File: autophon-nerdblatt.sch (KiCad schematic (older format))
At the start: 2 parts

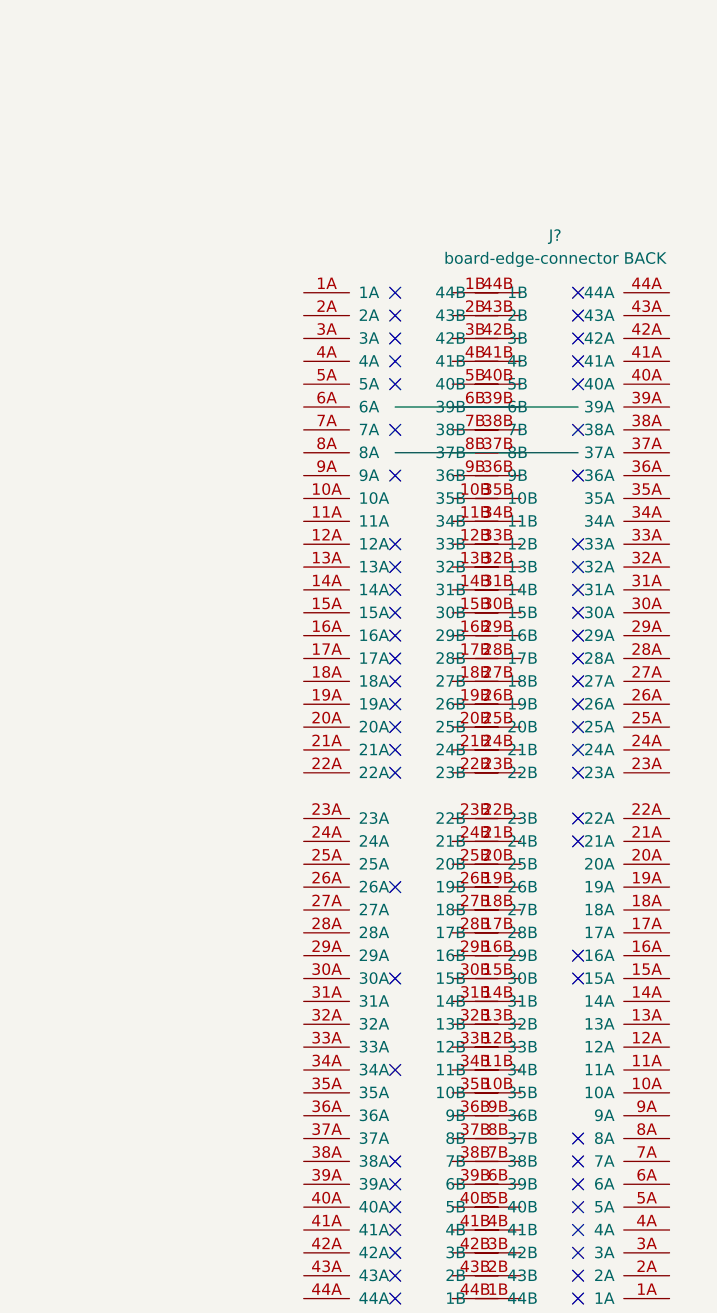
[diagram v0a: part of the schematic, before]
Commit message: measured pinout, added lables accordingly
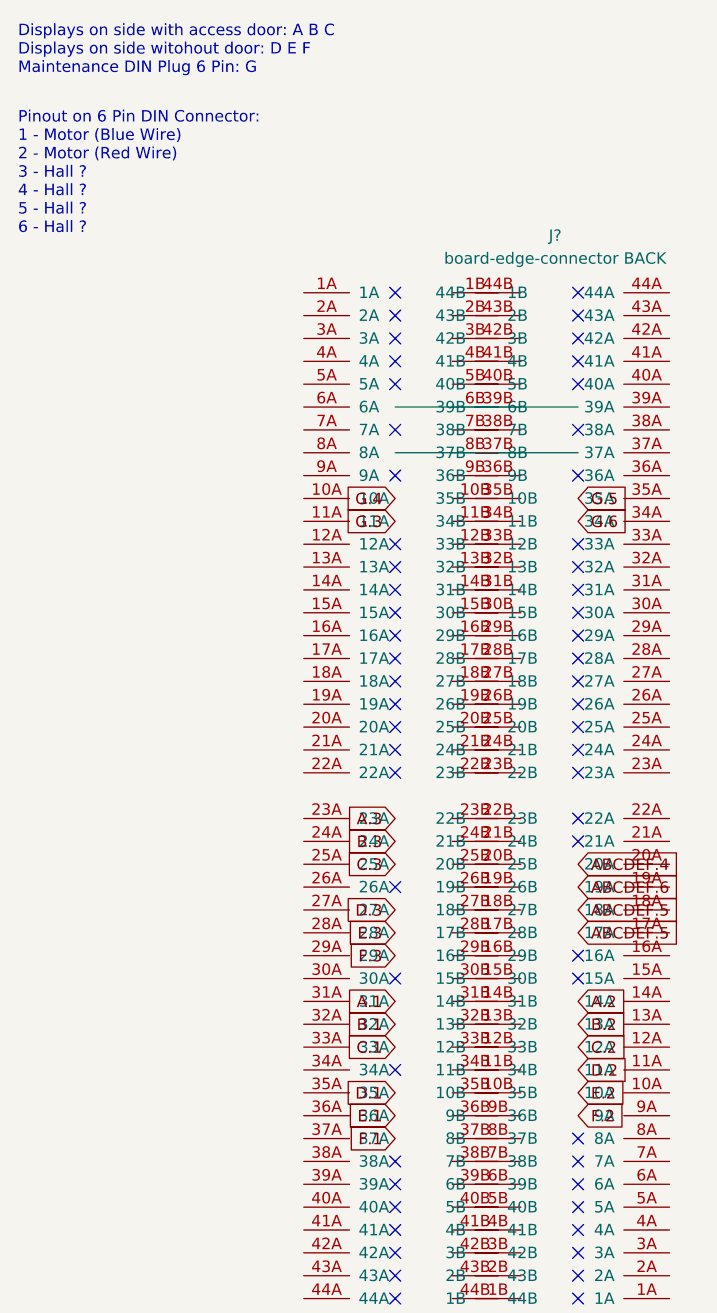
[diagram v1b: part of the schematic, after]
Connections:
- net labels added: A.1, A.2, A.3, ABCDEF.4, ABCDEF.5, ABCDEF.6, B.1, B.2, B.3, C.1, C.2, C.3, D.1, D.2, D.3, E.1, E.2, E.3, F.1, F.2, F.3, G.3, G.4, G.5, G.6
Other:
- note added: "Displays on side with access door: A B C\nDisplays on side witohout door: D E F\nMaintenance DIN Plug 6 Pin: G"
- note added: "Pinout on 6 Pin DIN Connector: \n1 - Motor (Blue Wire)\n2 - Motor (Red Wire)\n3 - Hall ?\n4 - Hall ? \n5 - Hall ? \n6 - Hall ?"
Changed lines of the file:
@@
 Wire Wire Line
 	2200 2450 3000 2450
+Text GLabel 2200 2650 0    50   Input ~ 0
+G.4
+Text GLabel 2200 2750 0    50   Input ~ 0
+G.3
+Text Notes 550  800  0    50   ~ 0
+Displays on side with access door: A B C\nDisplays on side witohout door: D E F\nMaintenance DIN Plug 6 Pin: G
+Text Notes 550  1500 0    50   ~ 0
+Pinout on 6 Pin DIN Connector: \n1 - Motor (Blue Wire)\n2 - Motor (Red Wire)\n3 - Hall ?\n4 - Hall ? \n5 - Hall ? \n6 - Hall ?
+Text GLabel 2200 4050 0    50   Input ~ 0
+A.3
+Text GLabel 2200 4150 0    50   Input ~ 0
+B.3
+Text GLabel 2200 4250 0    50   Input ~ 0
+C.3
+Text GLabel 2200 4450 0    50   Input ~ 0
+D.3
+Text GLabel 2200 4550 0    50   Input ~ 0
+E.3
+Text GLabel 2200 4650 0    50   Input ~ 0
+F.3
+Text GLabel 2200 4850 0    50   Input ~ 0
+A.1
+Text GLabel 2200 4950 0    50   Input ~ 0
+B.1
+Text GLabel 2200 5050 0    50   Input ~ 0
+C.1
+Text GLabel 2200 5250 0    50   Input ~ 0
+D.1
+Text GLabel 2200 5350 0    50   Input ~ 0
+E.1
+Text GLabel 2200 5450 0    50   Input ~ 0
+F.1
+Text GLabel 3000 5350 2    50   Input ~ 0
+F.2
+Text GLabel 3000 5250 2    50   Input ~ 0
+E.2
+Text GLabel 3000 5150 2    50   Input ~ 0
+D.2
+Text GLabel 3000 5050 2    50   Input ~ 0
+C.2
+Text GLabel 3000 4950 2    50   Input ~ 0
+B.2
+Text GLabel 3000 4850 2    50   Input ~ 0
+A.2
+Text GLabel 3000 4550 2    50   Input ~ 0
+ABCDEF.5
+Text GLabel 3000 4450 2    50   Input ~ 0
+ABCDEF.5
+Text GLabel 3000 4350 2    50   Input ~ 0
+ABCDEF.6
+Text GLabel 3000 4250 2    50   Input ~ 0
+ABCDEF.4
+Text GLabel 3000 2750 2    50   Input ~ 0
+G.6
+Text GLabel 3000 2650 2    50   Input ~ 0
+G.5
 $EndSCHEMATC

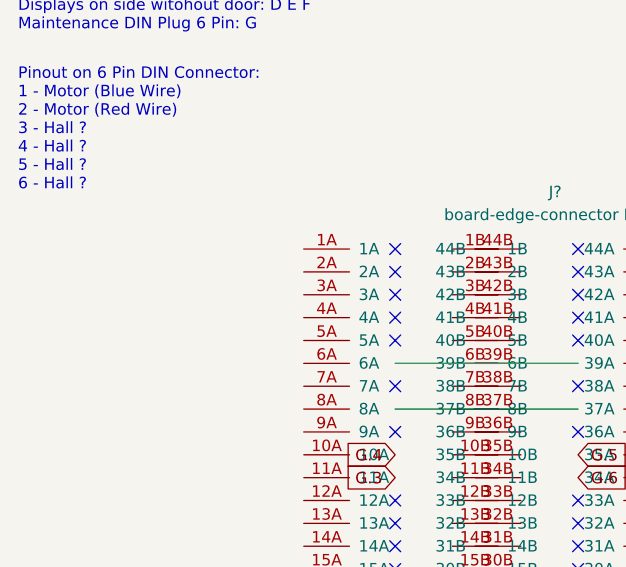
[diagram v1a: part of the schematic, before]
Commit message: added DIN 6 pin reference
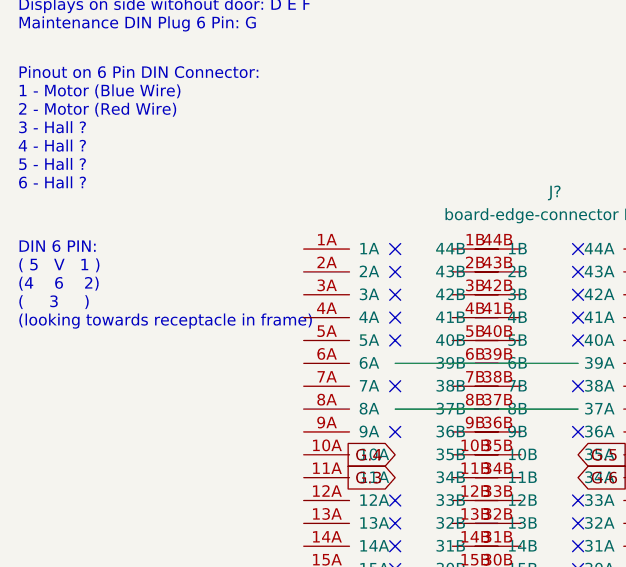
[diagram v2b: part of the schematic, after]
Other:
- note added: "DIN 6 PIN:\n( 5 V 1 )\n(4 6 2)\n( 3 )\n(looking towards receptacle in frame)"
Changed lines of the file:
@@
 Text GLabel 3000 2650 2    50   Input ~ 0
 G.5
+Text Notes 550  2100 0    50   ~ 0
+DIN 6 PIN:\n( 5   V   1 )\n(4    6    2)\n(     3     )\n(looking towards receptacle in frame)
 $EndSCHEMATC

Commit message: Symbol, Footprint improvements. Default Board
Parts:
- removed J?: board-edge-connector FRONT, symbol autophon-nerdblatt:board-edge-connector
- removed J?: board-edge-connector BACK, symbol autophon-nerdblatt:board-edge-connector
- added J1: board-edge-connector, autophon-nerdblatt:autophon-pcb-edge-connector, symbol autophon-nerdblatt:board-edge-connector
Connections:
- wire segments 2 -> 36
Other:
- note added: "xA=TopLayer\nxB=BotLayer"

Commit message: schaltplan aufgeteilt, hallsensorboard erstellt, getestete logic in FF.sch erstellt.
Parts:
- added U2, U3, U4: L298HN, Package_TO_SOT_THT:TO-220F-15_P2.54x5.08mm_StaggerOdd_Lead5.08mm_Vertical, symbol Driver_Motor:L298HN
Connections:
- net A.1: now also U2.2 (OUT1)
- net A.2: now also U2.3 (OUT2)
- net B.1: now also U2.13 (OUT3)
- net B.2: now also U2.14 (OUT4)
- net C.1: now also U3.2 (OUT1)
- net C.2: now also U3.3 (OUT2)
- net D.1: now also U3.13 (OUT3)
- net D.2: now also U3.14 (OUT4)
- net E.1: now also U4.2 (OUT1)
- net E.2: now also U4.3 (OUT2)
- net F.1: now also U4.13 (OUT3)
- net F.2: now also U4.14 (OUT4)
- new net A_EN: U2.6 (EnA)
- new net A_IN1: U2.5 (IN1)
- new net A_IN2: U2.7 (IN2)
- new net B_EN: U2.11 (EnB)
- new net B_IN3: U2.10 (IN3)
- new net B_IN4: U2.12 (IN4)
- new net C_EN: U3.6 (EnA)
- new net C_IN1: U3.5 (IN1)
- new net C_IN2: U3.7 (IN2)
- new net D_EN: U3.11 (EnB)
- new net D_IN3: U3.10 (IN3)
- new net D_IN4: U3.12 (IN4)
- new net E_EN: U4.6 (EnA)
- new net E_IN1: U4.5 (IN1)
- new net E_IN2: U4.7 (IN2)
- new net F_EN: U4.11 (EnB)
- new net F_IN3: U4.10 (IN3)
- new net F_IN4: U4.12 (IN4)
- new net GND1: U2.8 (GND), U3.8 (GND), U4.8 (GND)
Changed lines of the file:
@@
 $Descr A4 11693 8268
 encoding utf-8
-Sheet 1 1
+Sheet 1 2
 Title ""
 Date ""
@@
 	1    0    0    -1
 $EndComp
+$Comp
+L Driver_Motor:L298HN U2
+U 1 1 5F63A398
+P 10050 1500
+F 0 "U2" H 10050 2381 50  0000 C CNN
+F 1 "L298HN" H 10050 2290 50  0000 C CNN
+F 2 "Package_TO_SOT_THT:TO-220F-15_P2.54x5.08mm_StaggerOdd_Lead5.08mm_Vertical" H 10100 850 50  0001 L CNN
+F 3 "http://www.st.com/st-web-ui/static/active/en/resource/technical/document/datasheet/CD00000240.pdf" H 10200 1750 50  0001 C CNN
+	1    10050 1500
+	1    0    0    -1
+$EndComp
+$Comp
+L Driver_Motor:L298HN U3
+U 1 1 5F63E13A
+P 10050 3450
+F 0 "U3" H 10050 4331 50  0000 C CNN
+F 1 "L298HN" H 10050 4240 50  0000 C CNN
+F 2 "Package_TO_SOT_THT:TO-220F-15_P2.54x5.08mm_StaggerOdd_Lead5.08mm_Vertical" H 10100 2800 50  0001 L CNN
+F 3 "http://www.st.com/st-web-ui/static/active/en/resource/technical/document/datasheet/CD00000240.pdf" H 10200 3700 50  0001 C CNN
+	1    10050 3450
+	1    0    0    -1
+$EndComp
+$Comp
+L Driver_Motor:L298HN U4
+U 1 1 5F63E70D
+P 10050 5400
+F 0 "U4" H 10050 6281 50  0000 C CNN
+F 1 "L298HN" H 10050 6190 50  0000 C CNN
+F 2 "Package_TO_SOT_THT:TO-220F-15_P2.54x5.08mm_StaggerOdd_Lead5.08mm_Vertical" H 10100 4750 50  0001 L CNN
+F 3 "http://www.st.com/st-web-ui/static/active/en/resource/technical/document/datasheet/CD00000240.pdf" H 10200 5650 50  0001 C CNN
+	1    10050 5400
+	1    0    0    -1
+$EndComp
+Wire Wire Line
+	10650 1300 10850 1300
+Wire Wire Line
+	10650 1400 10850 1400
+Wire Wire Line
+	10650 1600 10850 1600
+Wire Wire Line
+	10650 1700 10850 1700
+Wire Wire Line
+	10650 3250 10850 3250
+Wire Wire Line
+	10650 3350 10850 3350
+Wire Wire Line
+	10650 3550 10850 3550
+Wire Wire Line
+	10650 3650 10850 3650
+Wire Wire Line
+	10650 5200 10850 5200
+Wire Wire Line
+	10650 5300 10850 5300
+Wire Wire Line
+	10650 5500 10850 5500
+Wire Wire Line
+	10650 5600 10850 5600
+Text GLabel 10850 1300 2    50   Input ~ 0
+A.1
+Text GLabel 10850 1400 2    50   Input ~ 0
+A.2
+Text GLabel 10850 1600 2    50   Input ~ 0
+B.1
+Text GLabel 10850 1700 2    50   Input ~ 0
+B.2
+Text GLabel 10850 3250 2    50   Input ~ 0
+C.1
+Text GLabel 10850 3350 2    50   Input ~ 0
+C.2
+Text GLabel 10850 3550 2    50   Input ~ 0
+D.1
+Text GLabel 10850 3650 2    50   Input ~ 0
+D.2
+Text GLabel 10850 5200 2    50   Input ~ 0
+E.1
+Text GLabel 10850 5300 2    50   Input ~ 0
+E.2
+Text GLabel 10850 5500 2    50   Input ~ 0
+F.1
+Text GLabel 10850 5600 2    50   Input ~ 0
+F.2
+$Comp
+L power:GND1 #PWR03
+U 1 1 5F64D2D4
+P 10050 6150
+F 0 "#PWR03" H 10050 5900 50  0001 C CNN
+F 1 "GND1" H 10055 5977 50  0000 C CNN
+F 2 "" H 10050 6150 50  0001 C CNN
+F 3 "" H 10050 6150 50  0001 C CNN
+	1    10050 6150
+	1    0    0    -1
+$EndComp
+$Comp
+L power:GND1 #PWR02
+U 1 1 5F64DB15
+P 10050 4200
+F 0 "#PWR02" H 10050 3950 50  0001 C CNN
+F 1 "GND1" H 10055 4027 50  0000 C CNN
+F 2 "" H 10050 4200 50  0001 C CNN
+F 3 "" H 10050 4200 50  0001 C CNN
+	1    10050 4200
+	1    0    0    -1
+$EndComp
+$Comp
+L power:GND1 #PWR01
+U 1 1 5F64DF75
+P 10050 2250
+F 0 "#PWR01" H 10050 2000 50  0001 C CNN
+F 1 "GND1" H 10055 2077 50  0000 C CNN
+F 2 "" H 10050 2250 50  0001 C CNN
+F 3 "" H 10050 2250 50  0001 C CNN
+	1    10050 2250
+	1    0    0    -1
+$EndComp
+Wire Wire Line
+	10050 6100 10050 6150
+Wire Wire Line
+	10050 2200 10050 2250
+Wire Wire Line
+	10050 4150 10050 4200
+Wire Wire Line
+	9450 1000 9350 1000
+Wire Wire Line
+	9450 1100 9350 1100
+Wire Wire Line
+	9450 1200 9350 1200
+Wire Wire Line
+	9450 1400 9350 1400
+Wire Wire Line
+	9450 1500 9350 1500
+Wire Wire Line
+	9450 1600 9350 1600
+Wire Wire Line
+	9450 2950 9300 2950
+Wire Wire Line
+	9450 3050 9300 3050
+Wire Wire Line
+	9450 3150 9300 3150
+Wire Wire Line
+	9450 3350 9300 3350
+Wire Wire Line
+	9450 3450 9300 3450
+Wire Wire Line
+	9450 3550 9300 3550
+Wire Wire Line
+	9450 4900 9300 4900
+Wire Wire Line
+	9450 5000 9300 5000
+Wire Wire Line
+	9450 5100 9300 5100
+Wire Wire Line
+	9450 5300 9300 5300
+Wire Wire Line
+	9450 5400 9300 5400
+Wire Wire Line
+	9450 5500 9300 5500
+Text GLabel 9350 1000 0    50   Input ~ 0
+A_IN1
+Text GLabel 9350 1100 0    50   Input ~ 0
+A_IN2
+Text GLabel 9350 1200 0    50   Input ~ 0
+A_EN
+Text GLabel 9350 1400 0    50   Input ~ 0
+B_IN3
+Text GLabel 9350 1500 0    50   Input ~ 0
+B_IN4
+Text GLabel 9350 1600 0    50   Input ~ 0
+B_EN
+Text GLabel 9300 2950 0    50   Input ~ 0
+C_IN1
+Text GLabel 9300 3050 0    50   Input ~ 0
+C_IN2
+Text GLabel 9300 3150 0    50   Input ~ 0
+C_EN
+Text GLabel 9300 3350 0    50   Input ~ 0
+D_IN3
+Text GLabel 9300 3450 0    50   Input ~ 0
+D_IN4
+Text GLabel 9300 3550 0    50   Input ~ 0
+D_EN
+Text GLabel 9300 4900 0    50   Input ~ 0
+E_IN1
+Text GLabel 9300 5000 0    50   Input ~ 0
+E_IN2
+Text GLabel 9300 5100 0    50   Input ~ 0
+E_EN
+Text GLabel 9300 5300 0    50   Input ~ 0
+F_IN3
+Text GLabel 9300 5400 0    50   Input ~ 0
+F_IN4
+Text GLabel 9300 5500 0    50   Input ~ 0
+F_EN
+$Sheet
+S 5950 750  1050 1350
+U 5F6AFC19
+F0 "FlipFlop_Logic" 50
+F1 "FF.sch" 50
+$EndSheet
 $EndSCHEMATC

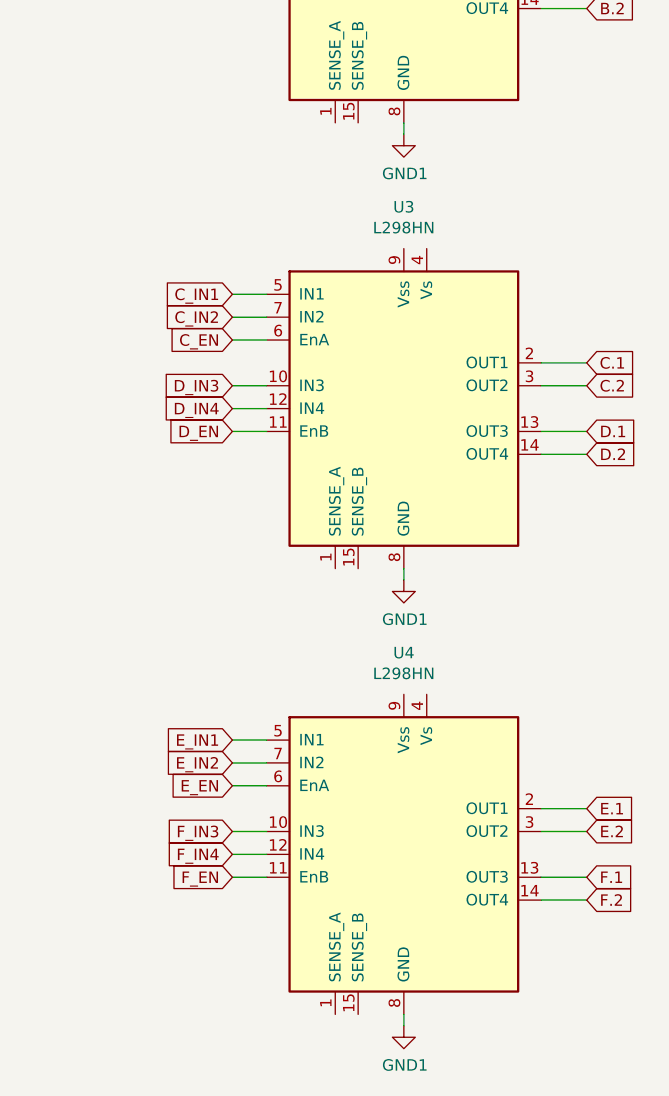
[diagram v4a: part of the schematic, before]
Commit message: first Routing of FF
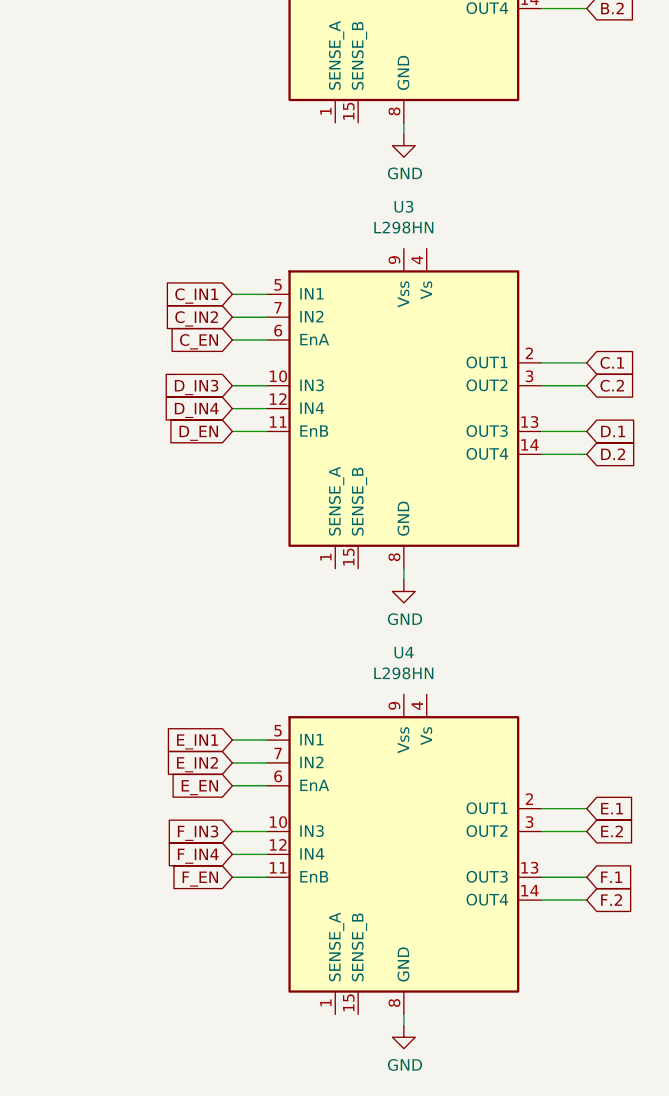
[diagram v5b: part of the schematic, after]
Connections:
- net GND1 renamed GND
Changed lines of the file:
@@
 Text GLabel 10850 5600 2    50   Input ~ 0
 F.2
-$Comp
-L power:GND1 #PWR03
-U 1 1 5F64D2D4
-P 10050 6150
-F 0 "#PWR03" H 10050 5900 50  0001 C CNN
-F 1 "GND1" H 10055 5977 50  0000 C CNN
-F 2 "" H 10050 6150 50  0001 C CNN
-F 3 "" H 10050 6150 50  0001 C CNN
-	1    10050 6150
-	1    0    0    -1
-$EndComp
-$Comp
-L power:GND1 #PWR02
-U 1 1 5F64DB15
-P 10050 4200
-F 0 "#PWR02" H 10050 3950 50  0001 C CNN
-F 1 "GND1" H 10055 4027 50  0000 C CNN
-F 2 "" H 10050 4200 50  0001 C CNN
-F 3 "" H 10050 4200 50  0001 C CNN
-	1    10050 4200
-	1    0    0    -1
-$EndComp
-$Comp
-L power:GND1 #PWR01
-U 1 1 5F64DF75
-P 10050 2250
-F 0 "#PWR01" H 10050 2000 50  0001 C CNN
-F 1 "GND1" H 10055 2077 50  0000 C CNN
-F 2 "" H 10050 2250 50  0001 C CNN
-F 3 "" H 10050 2250 50  0001 C CNN
-	1    10050 2250
-	1    0    0    -1
-$EndComp
 Wire Wire Line
 	10050 6100 10050 6150
@@
 F1 "FF.sch" 50
 $EndSheet
+$Comp
+L power:GND #PWR?
+U 1 1 5FC57AD7
+P 10050 2250
+F 0 "#PWR?" H 10050 2000 50  0001 C CNN
+F 1 "GND" H 10055 2077 50  0000 C CNN
+F 2 "" H 10050 2250 50  0001 C CNN
+F 3 "" H 10050 2250 50  0001 C CNN
+	1    10050 2250
+	1    0    0    -1
+$EndComp
+$Comp
+L power:GND #PWR?
+U 1 1 5FC58737
+P 10050 4200
+F 0 "#PWR?" H 10050 3950 50  0001 C CNN
+F 1 "GND" H 10055 4027 50  0000 C CNN
+F 2 "" H 10050 4200 50  0001 C CNN
+F 3 "" H 10050 4200 50  0001 C CNN
+	1    10050 4200
+	1    0    0    -1
+$EndComp
+$Comp
+L power:GND #PWR?
+U 1 1 5FC591D3
+P 10050 6150
+F 0 "#PWR?" H 10050 5900 50  0001 C CNN
+F 1 "GND" H 10055 5977 50  0000 C CNN
+F 2 "" H 10050 6150 50  0001 C CNN
+F 3 "" H 10050 6150 50  0001 C CNN
+	1    10050 6150
+	1    0    0    -1
+$EndComp
 $EndSCHEMATC

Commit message: Thinking.
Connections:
- net A.1: no longer J1.31A
- net A.2: no longer J1.14B
- net B.1: no longer J1.32A
- net B.2: no longer J1.13B
- net C.1: no longer J1.33A
- net C.2: no longer J1.12B
- net D.1: no longer J1.35A
- net D.2: no longer J1.11B
- net E.1: no longer J1.36A
- net E.2: no longer J1.10B
- net F.1: no longer J1.37A
- net F.2: no longer J1.9B
- net A.3 renamed A_HALL_VCC
- net ABCDEF.4 renamed ABCDEF_HALL_INDEX
- net ABCDEF.5 renamed ABCDEF_HALL_GND
- net ABCDEF.6 renamed ABCDEF_HALL_ROTOR
- net B.3 renamed B_HALL_VCC
- net C.3 renamed C_HALL_VCC
- net D.3 renamed D_HALL_VCC
- net E.3 renamed E_HALL_VCC
- net F.3 renamed F_HALL_VCC
- new net A_MOTOR_NEG: J1.14B
- new net A_MOTOR_POS: J1.31A
- new net B_MOTOR_NEG: J1.13B
- new net B_MOTOR_POS: J1.32A
- new net C_MOTOR_NEG: J1.12B
- new net C_MOTOR_POS: J1.33A
- new net D_MOTOR_NEG: J1.11B
- new net D_MOTOR_POS: J1.35A
- new net E_MOTOR_NEG: J1.10B
- new net E_MOTOR_POS: J1.36A
- new net F_MOTOR_NEG: J1.9B
- new net F_MOTOR_POS: J1.37A
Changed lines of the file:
@@
 $Descr A4 11693 8268
 encoding utf-8
-Sheet 1 2
+Sheet 1 3
 Title ""
 Date ""
@@
 G.3
 Text GLabel 3350 4200 0    50   Input ~ 0
-A.3
+A_HALL_VCC
 Text GLabel 3350 4300 0    50   Input ~ 0
-B.3
+B_HALL_VCC
 Text GLabel 3350 4400 0    50   Input ~ 0
-C.3
+C_HALL_VCC
 Text GLabel 3350 4600 0    50   Input ~ 0
-D.3
+D_HALL_VCC
 Text GLabel 3350 4700 0    50   Input ~ 0
-E.3
+E_HALL_VCC
 Text GLabel 3350 4800 0    50   Input ~ 0
-F.3
+F_HALL_VCC
 Text GLabel 3350 5000 0    50   Input ~ 0
-A.1
+A_MOTOR_POS
 Text GLabel 3350 5100 0    50   Input ~ 0
-B.1
+B_MOTOR_POS
 Text GLabel 3350 5200 0    50   Input ~ 0
-C.1
+C_MOTOR_POS
 Text GLabel 3350 5400 0    50   Input ~ 0
-D.1
+D_MOTOR_POS
 Text GLabel 3350 5500 0    50   Input ~ 0
-E.1
+E_MOTOR_POS
 Text GLabel 3350 5600 0    50   Input ~ 0
-F.1
+F_MOTOR_POS
 Text GLabel 4550 5500 2    50   Input ~ 0
-F.2
+F_MOTOR_NEG
 Text GLabel 4550 5400 2    50   Input ~ 0
-E.2
+E_MOTOR_NEG
 Text GLabel 4550 5300 2    50   Input ~ 0
-D.2
+D_MOTOR_NEG
 Text GLabel 4550 5200 2    50   Input ~ 0
-C.2
+C_MOTOR_NEG
 Text GLabel 4550 5100 2    50   Input ~ 0
-B.2
+B_MOTOR_NEG
 Text GLabel 4550 5000 2    50   Input ~ 0
-A.2
+A_MOTOR_NEG
 Text GLabel 4550 4700 2    50   Input ~ 0
-ABCDEF.5
+ABCDEF_HALL_GND
 Text GLabel 4500 2800 2    50   Input ~ 0
 G.5
@@
 G.6
 Text GLabel 4550 4600 2    50   Input ~ 0
-ABCDEF.5
+ABCDEF_HALL_GND
 Text GLabel 4550 4500 2    50   Input ~ 0
-ABCDEF.6
+ABCDEF_HALL_ROTOR
 Text GLabel 4550 4400 2    50   Input ~ 0
-ABCDEF.4
+ABCDEF_HALL_INDEX
 NoConn ~ 3450 4500
 NoConn ~ 3450 1900
@@
 	1    0    0    -1
 $EndComp
+$Sheet
+S 5950 2950 2450 1350
+U 5FC6F066
+F0 "dummy vogelchr" 50
+F1 "dummy_vogelchr.sch" 50
+$EndSheet
 $EndSCHEMATC
